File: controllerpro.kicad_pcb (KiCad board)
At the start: 2 copper layers, 92.7 x 88.3 mm, 26 parts, among them P0 Conn_01x08_Male, P1 Conn_01x08_Male, P2 Conn_01x08_Male, P3 Conn_01x08_Male

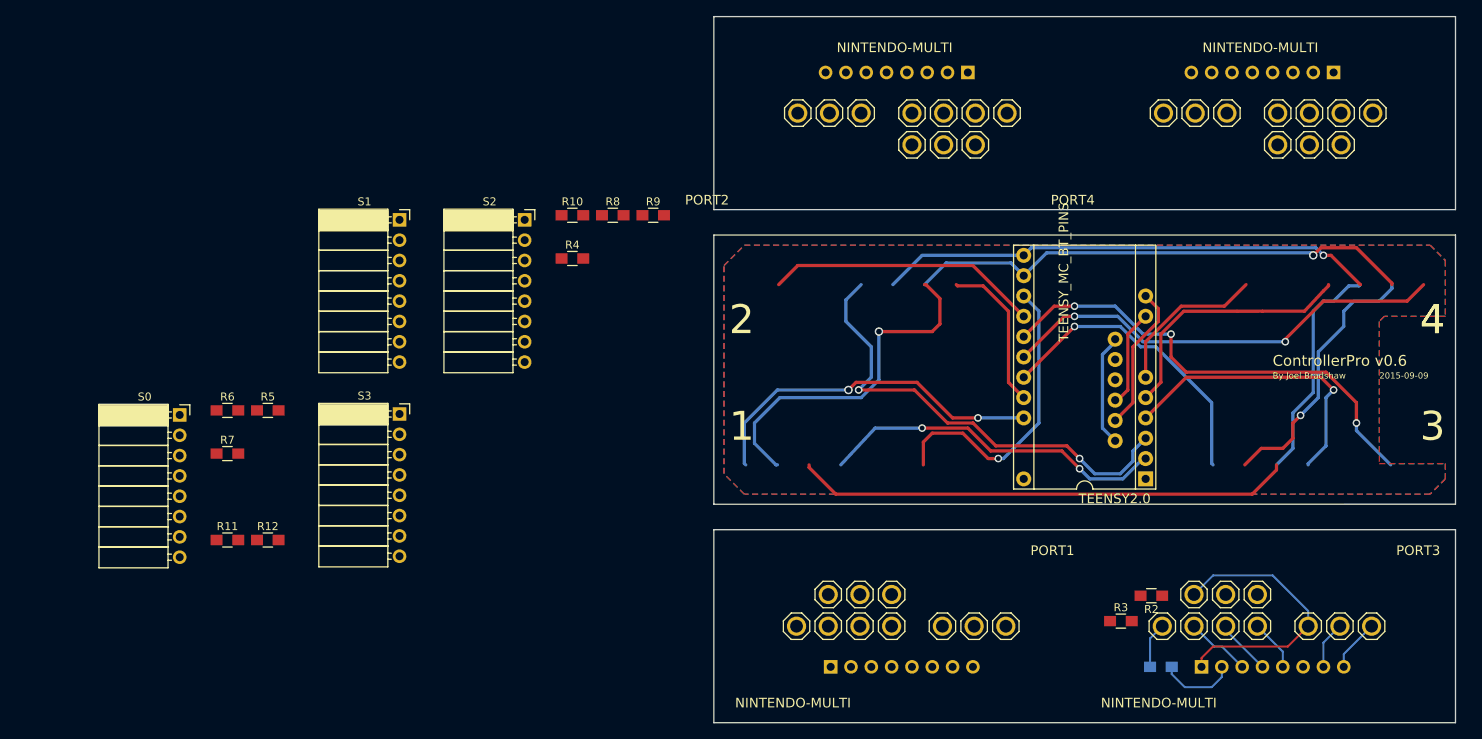
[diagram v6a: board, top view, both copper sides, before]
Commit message: Finish initial layout of first port
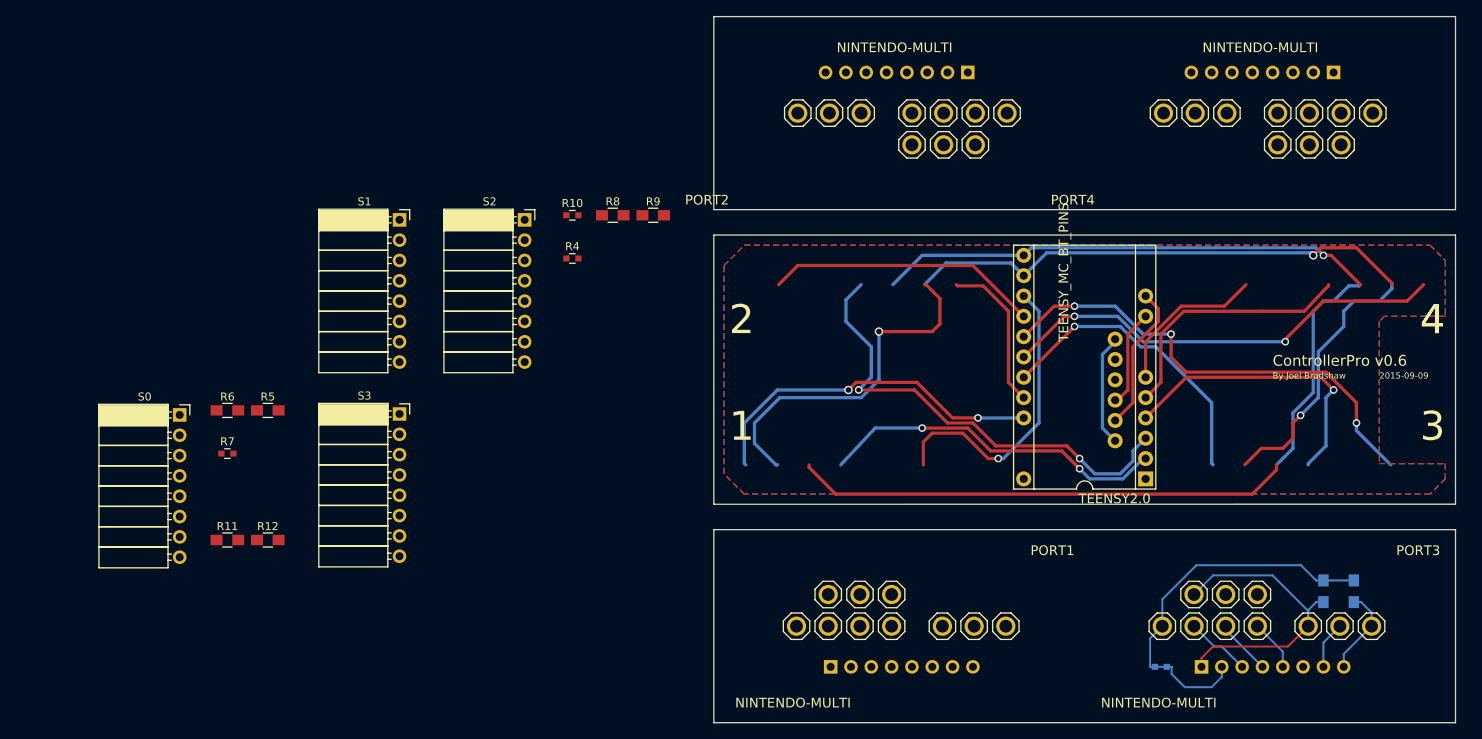
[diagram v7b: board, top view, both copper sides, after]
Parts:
- R1, R10, R4, R7: footprint Resistors_SMD:R_0805_HandSoldering -> Capacitors_SMD:C_0603
- R2, R3: moved to B.Cu
- moved R3 29.4 mm to (181.6, 133.4), turned to 90 degrees
- moved R2 21.5 mm to (177.8, 133.4), turned to 90 degrees
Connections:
- PORT1 pad 1: Net-(PORT1-Pad1) -> Net-(P2-Pad2)
- PORT2 pad 1: Net-(PORT2-Pad1) -> Net-(P3-Pad2)
- PORT3 pad 1: Net-(PORT3-Pad1) -> Net-(P0-Pad2)
- PORT4 pad 1: Net-(PORT4-Pad1) -> Net-(P1-Pad2)
- R1 pad 2: Net-(PORT3-Pad1) -> Net-(P0-Pad2)
- R10 pad 2: Net-(PORT2-Pad1) -> Net-(P3-Pad2)
- R11 pad 2: Net-(PORT2-Pad1) -> Net-(P3-Pad2)
- R12 pad 2: Net-(PORT2-Pad1) -> Net-(P3-Pad2)
- R2 pad 2: Net-(PORT3-Pad1) -> Net-(P0-Pad2)
- R3 pad 2: Net-(PORT3-Pad1) -> Net-(P0-Pad2)
- R4 pad 2: Net-(PORT4-Pad1) -> Net-(P1-Pad2)
- R5 pad 2: Net-(PORT4-Pad1) -> Net-(P1-Pad2)
- R6 pad 2: Net-(PORT4-Pad1) -> Net-(P1-Pad2)
- R7 pad 2: Net-(PORT1-Pad1) -> Net-(P2-Pad2)
- R8 pad 2: Net-(PORT1-Pad1) -> Net-(P2-Pad2)
- R9 pad 2: Net-(PORT1-Pad1) -> Net-(P2-Pad2)
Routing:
- net Net-(P0-Pad2): track 9.65 -> 47.9 mm
- net Net-(PORT3-Pad1): track 5.71 -> 0.00 mm
- net Net-(P0-Pad8): track 6.52 -> 11.0 mm
- net Net-(P0-Pad1): track 35.1 -> 39.4 mm

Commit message: Fix port numbers
That was annoying, but fine
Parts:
- removed PORT4: NINTENDO-MULTI, NINTENDO-MULTI
- added PORT0: NINTENDO-MULTI, NINTENDO-MULTI, F.Cu at (169.5, 137.8)
- moved PORT1 80.3 mm to (172.1, 73.7), turned to 180 degrees
- moved PORT3 77.3 mm to (126.4, 73.7), turned to 180 degrees
- moved PORT2 64.2 mm to (123.8, 137.8), turned to 0 degrees
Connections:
- PORT1 pad 1: Net-(P2-Pad2) -> Net-(P1-Pad2)
- PORT1 pad 10: Net-(P2-Pad1) -> Net-(P1-Pad1)
- PORT1 pad 2: Net-(P2-Pad3) -> Net-(P1-Pad3)
- PORT1 pad 3: Net-(P2-Pad4) -> Net-(P1-Pad4)
- PORT1 pad 4: Net-(P2-Pad5) -> Net-(P1-Pad5)
- PORT1 pad 5: Net-(P2-Pad1) -> Net-(P1-Pad1)
- PORT1 pad 6: Net-(P2-Pad7) -> Net-(P1-Pad7)
- PORT1 pad 7: Net-(P2-Pad8) -> Net-(P1-Pad8)
- PORT2 pad 1: Net-(P3-Pad2) -> Net-(P2-Pad2)
- PORT2 pad 10: Net-(P3-Pad1) -> Net-(P2-Pad1)
- PORT2 pad 2: Net-(P3-Pad3) -> Net-(P2-Pad3)
- PORT2 pad 3: Net-(P3-Pad4) -> Net-(P2-Pad4)
- PORT2 pad 4: Net-(P3-Pad5) -> Net-(P2-Pad5)
- PORT2 pad 5: Net-(P3-Pad1) -> Net-(P2-Pad1)
- PORT2 pad 6: Net-(P3-Pad7) -> Net-(P2-Pad7)
- PORT2 pad 7: Net-(P3-Pad8) -> Net-(P2-Pad8)
- PORT3 pad 1: Net-(P0-Pad2) -> Net-(P3-Pad2)
- PORT3 pad 10: Net-(P0-Pad1) -> Net-(P3-Pad1)
- PORT3 pad 2: Net-(P0-Pad3) -> Net-(P3-Pad3)
- PORT3 pad 3: Net-(P0-Pad4) -> Net-(P3-Pad4)
- PORT3 pad 4: Net-(P0-Pad5) -> Net-(P3-Pad5)
- PORT3 pad 5: Net-(P0-Pad1) -> Net-(P3-Pad1)
- PORT3 pad 6: Net-(P0-Pad7) -> Net-(P3-Pad7)
- PORT3 pad 7: Net-(P0-Pad8) -> Net-(P3-Pad8)
